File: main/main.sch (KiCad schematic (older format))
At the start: 9 parts

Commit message: picked microcontroller - stm32f401RETx, started schematic, made LED array
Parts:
- removed G1: DOW, william_logos:dow_logo_10mm, symbol william_logos:DOW
- removed G2: MEC, william_logos:mec_small, symbol william_logos:MEC
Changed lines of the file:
@@
 $Descr A4 11693 8268
 encoding utf-8
-Sheet 1 1
+Sheet 1 3
 Title ""
 Date ""
@@
 $EndComp
 $Comp
-L william_logos:DOW G1
-U 1 1 5D9BA876
-P 5800 6700
-F 0 "G1" H 5825 6746 50  0000 L CNN
-F 1 "DOW" H 5825 6655 50  0000 L CNN
-F 2 "william_logos:dow_logo_10mm" H 5800 6800 50  0001 C CNN
-F 3 "" H 5800 6800 50  0001 C CNN
-	1    5800 6700
-	1    0    0    -1
-$EndComp
-$Comp
-L william_logos:MEC G2
-U 1 1 5D9BAA57
-P 5800 6900
-F 0 "G2" H 5825 6946 50  0000 L CNN
-F 1 "MEC" H 5825 6855 50  0000 L CNN
-F 2 "william_logos:mec_small" H 5800 6950 50  0001 C CNN
-F 3 "" H 5800 6950 50  0001 C CNN
-	1    5800 6900
-	1    0    0    -1
-$EndComp
-$Comp
 L william_dfa:Fiducial FID3
 U 1 1 5D9BDAFA
@@
 	1    0    0    -1
 $EndComp
+$Sheet
+S 7500 3250 700  500
+U 5DEECD42
+F0 "LEDs" 50
+F1 "led_array.sch" 50
+F2 "5V" I L 7500 3350 50
+F3 "DIN" I L 7500 3500 50
+F4 "DOUT" O R 8200 3500 50
+F5 "GND" O L 7500 3650 50
+$EndSheet
+$Sheet
+S 3950 2050 1950 1000
+U 5F8F0BCD
+F0 "mic" 50
+F1 "../subs/stm32f401rbXX.sch" 50
+$EndSheet
 $EndSCHEMATC

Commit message: started layout to see if practical
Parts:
- removed FID1, FID2, FID3: Fiducial, Fiducial:Fiducial_1mm_Dia_2mm_Outer, symbol william_dfa:Fiducial
- added BT1: RTC battery, william_batteries:Keystone_3034_1x20mm-CoinCell, symbol Device:Battery_Cell
- added C1, C3: 100N, Capacitor_SMD:C_0603_1608Metric, symbol Device:C
- added C2: 10N, Capacitor_SMD:C_0603_1608Metric, symbol Device:C
- added C4: 10U, Capacitor_SMD:C_0603_1608Metric, symbol Device:C
- added J1: USB_B_Micro, Connector_USB:USB_Micro-B_GCT_USB3076-30-A, symbol Connector:USB_B_Micro
- added SW1, SW2, SW3, SW4, SW5, SW6: SW_SPST, Button_Switch_SMD:SW_Push_1P1T_NO_6x6mm_H9.5mm, symbol Switch:SW_SPST
- added U1: AP1117-33, Package_TO_SOT_SMD:SOT-223-3_TabPin2, symbol Regulator_Linear:AP1117-33
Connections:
- net labels added: +3V3, +5V, +BATT, GND, SWITCH0, SWITCH1, SWITCH2, SWITCH3, SWITCH4, SWITCH5
- wire segments 0 -> 55
- no-connect marks 0 -> 4

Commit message: most components
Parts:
- removed C2: 10N, Capacitor_SMD:C_0603_1608Metric, symbol Device:C
- C1, C3, C4: footprint Capacitor_SMD:C_0603_1608Metric -> Capacitor_SMD:C_0402_1005Metric
- H1, H2, H3, H4: footprint MountingHole:MountingHole_3mm_Pad_Via -> MountingHole:MountingHole_2.1mm
- SW1, SW2, SW3, SW4, SW5, SW6: footprint Button_Switch_SMD:SW_Push_1P1T_NO_6x6mm_H9.5mm -> william_switch:KAN4562-0501C
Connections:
- wire segments 55 -> 53
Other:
- note added: "brightness"
- note added: "hour+"
- note added: "hour-"
- note added: "min+"
- note added: "min-"
- note added: "mode"
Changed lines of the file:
@@
 $Descr A4 11693 8268
 encoding utf-8
-Sheet 1 3
+Sheet 1 4
 Title ""
 Date ""
@@
 F 0 "H1" H 6400 6746 50  0000 L CNN
 F 1 "MountingHole" H 6400 6655 50  0000 L CNN
-F 2 "MountingHole:MountingHole_3mm_Pad_Via" H 6300 6700 50  0001 C CNN
+F 2 "MountingHole:MountingHole_2.1mm" H 6300 6700 50  0001 C CNN
 F 3 "~" H 6300 6700 50  0001 C CNN
 	1    6300 6700
@@
 F 0 "H2" H 6400 7046 50  0000 L CNN
 F 1 "MountingHole" H 6400 6955 50  0000 L CNN
-F 2 "MountingHole:MountingHole_3mm_Pad_Via" H 6300 7000 50  0001 C CNN
+F 2 "MountingHole:MountingHole_2.1mm" H 6300 7000 50  0001 C CNN
 F 3 "~" H 6300 7000 50  0001 C CNN
 	1    6300 7000
@@
 F 0 "H3" H 6400 7346 50  0000 L CNN
 F 1 "MountingHole" H 6400 7255 50  0000 L CNN
-F 2 "MountingHole:MountingHole_3mm_Pad_Via" H 6300 7300 50  0001 C CNN
+F 2 "MountingHole:MountingHole_2.1mm" H 6300 7300 50  0001 C CNN
 F 3 "~" H 6300 7300 50  0001 C CNN
 	1    6300 7300
@@
 F 0 "H4" H 6400 7646 50  0000 L CNN
 F 1 "MountingHole" H 6400 7555 50  0000 L CNN
-F 2 "MountingHole:MountingHole_3mm_Pad_Via" H 6300 7600 50  0001 C CNN
+F 2 "MountingHole:MountingHole_2.1mm" H 6300 7600 50  0001 C CNN
 F 3 "~" H 6300 7600 50  0001 C CNN
 	1    6300 7600
@@
 F5 "GND" O L 6850 3650 50
 $EndSheet
-$Sheet
-S 4400 3150 1250 1150
-U 5F8F0BCD
-F0 "mic" 50
-F1 "../subs/stm32f401rbXX.sch" 50
-F2 "3V3" I L 4400 3250 50
-F3 "GND" I L 4400 4200 50
-F4 "VBAT" I L 4400 3350 50
-F5 "LED_DATA_OUT" O R 5650 3500 50
-F6 "SWITCH0" I L 4400 3500 50
-F7 "SWITCH1" I L 4400 3600 50
-F8 "SWITCH2" I L 4400 3700 50
-F9 "SWITCH3" I L 4400 3800 50
-F10 "SWITCH4" I L 4400 3900 50
-F11 "SWITCH5" I L 4400 4000 50
-$EndSheet
 $Comp
 L Device:Battery_Cell BT1
@@
 $EndComp
 $Comp
-L Device:C C2
-U 1 1 5F9F0D5F
-P 3200 1250
-F 0 "C2" H 3315 1296 50  0000 L CNN
-F 1 "10N" H 3315 1205 50  0000 L CNN
-F 2 "Capacitor_SMD:C_0603_1608Metric" H 3238 1100 50  0001 C CNN
-F 3 "~" H 3200 1250 50  0001 C CNN
-	1    3200 1250
-	1    0    0    -1
-$EndComp
-$Comp
 L Device:C C1
 U 1 1 5F9F1B83
@@
 F 0 "C1" H 2915 1296 50  0000 L CNN
 F 1 "100N" H 2915 1205 50  0000 L CNN
-F 2 "Capacitor_SMD:C_0603_1608Metric" H 2838 1100 50  0001 C CNN
+F 2 "Capacitor_SMD:C_0402_1005Metric" H 2838 1100 50  0001 C CNN
 F 3 "~" H 2800 1250 50  0001 C CNN
 	1    2800 1250
@@
 F 0 "C3" H 4215 1296 50  0000 L CNN
 F 1 "100N" H 4215 1205 50  0000 L CNN
-F 2 "Capacitor_SMD:C_0603_1608Metric" H 4138 1100 50  0001 C CNN
+F 2 "Capacitor_SMD:C_0402_1005Metric" H 4138 1100 50  0001 C CNN
 F 3 "~" H 4100 1250 50  0001 C CNN
 	1    4100 1250
@@
 F 0 "C4" H 4665 1296 50  0000 L CNN
 F 1 "10U" H 4665 1205 50  0000 L CNN
-F 2 "Capacitor_SMD:C_0603_1608Metric" H 4588 1100 50  0001 C CNN
+F 2 "Capacitor_SMD:C_0402_1005Metric" H 4588 1100 50  0001 C CNN
 F 3 "~" H 4550 1250 50  0001 C CNN
 	1    4550 1250
@@
 	1    0    0    -1
 $EndComp
-Wire Wire Line
-	2800 1400 3200 1400
-Connection ~ 3200 1400
-Wire Wire Line
-	3200 1400 3650 1400
 Connection ~ 3650 1400
 Wire Wire Line
@@
 Wire Wire Line
 	2800 1000 2800 1100
-Wire Wire Line
-	3350 1100 3200 1100
 Connection ~ 2800 1100
-Connection ~ 3200 1100
-Wire Wire Line
-	3200 1100 2800 1100
 $Comp
 L power:+3V3 #PWR011
@@
 $EndComp
 $Comp
-L Switch:SW_SPST SW6
-U 1 1 5FA1FE73
-P 1350 5900
-F 0 "SW6" H 1350 6135 50  0000 C CNN
-F 1 "SW_SPST" H 1350 6044 50  0000 C CNN
-F 2 "Button_Switch_SMD:SW_Push_1P1T_NO_6x6mm_H9.5mm" H 1350 5900 50  0001 C CNN
-F 3 "~" H 1350 5900 50  0001 C CNN
-	1    1350 5900
-	1    0    0    -1
-$EndComp
-$Comp
-L Switch:SW_SPST SW5
-U 1 1 5FA1FE69
-P 1350 5500
-F 0 "SW5" H 1350 5735 50  0000 C CNN
-F 1 "SW_SPST" H 1350 5644 50  0000 C CNN
-F 2 "Button_Switch_SMD:SW_Push_1P1T_NO_6x6mm_H9.5mm" H 1350 5500 50  0001 C CNN
-F 3 "~" H 1350 5500 50  0001 C CNN
-	1    1350 5500
-	1    0    0    -1
-$EndComp
-$Comp
-L Switch:SW_SPST SW4
-U 1 1 5FA1E15D
-P 1350 5100
-F 0 "SW4" H 1350 5335 50  0000 C CNN
-F 1 "SW_SPST" H 1350 5244 50  0000 C CNN
-F 2 "Button_Switch_SMD:SW_Push_1P1T_NO_6x6mm_H9.5mm" H 1350 5100 50  0001 C CNN
-F 3 "~" H 1350 5100 50  0001 C CNN
-	1    1350 5100
-	1    0    0    -1
-$EndComp
-$Comp
-L Switch:SW_SPST SW3
-U 1 1 5FA1E153
-P 1350 4700
-F 0 "SW3" H 1350 4935 50  0000 C CNN
-F 1 "SW_SPST" H 1350 4844 50  0000 C CNN
-F 2 "Button_Switch_SMD:SW_Push_1P1T_NO_6x6mm_H9.5mm" H 1350 4700 50  0001 C CNN
-F 3 "~" H 1350 4700 50  0001 C CNN
-	1    1350 4700
-	1    0    0    -1
-$EndComp
-$Comp
-L Switch:SW_SPST SW2
-U 1 1 5FA1CE3B
-P 1350 4300
-F 0 "SW2" H 1350 4535 50  0000 C CNN
-F 1 "SW_SPST" H 1350 4444 50  0000 C CNN
-F 2 "Button_Switch_SMD:SW_Push_1P1T_NO_6x6mm_H9.5mm" H 1350 4300 50  0001 C CNN
-F 3 "~" H 1350 4300 50  0001 C CNN
-	1    1350 4300
-	1    0    0    -1
-$EndComp
-$Comp
 L Switch:SW_SPST SW1
 U 1 1 5FA1CA8C
@@
 F 0 "SW1" H 1350 4135 50  0000 C CNN
 F 1 "SW_SPST" H 1350 4044 50  0000 C CNN
-F 2 "Button_Switch_SMD:SW_Push_1P1T_NO_6x6mm_H9.5mm" H 1350 3900 50  0001 C CNN
+F 2 "william_switch:KAN4562-0501C" H 1350 3900 50  0001 C CNN
 F 3 "~" H 1350 3900 50  0001 C CNN
 	1    1350 3900
@@
 Text Label 3850 3800 0    50   ~ 0
 SWITCH3
-Text Label 3850 3900 0    50   ~ 0
-SWITCH4
-Text Label 3850 4000 0    50   ~ 0
-SWITCH5
 Wire Wire Line
 	4400 3500 3850 3500
@@
 Wire Wire Line
 	3850 3800 4400 3800
-Wire Wire Line
-	4400 3900 3850 3900
-Wire Wire Line
-	3850 4000 4400 4000
 NoConn ~ 1650 1350
 NoConn ~ 1650 1450
@@
 	1    0    0    -1
 $EndComp
+$Sheet
+S 4400 3150 1250 1150
+U 5F8F0BCD
+F0 "mic" 50
+F1 "../subs/STM32F401CBUxX.sch" 50
+F2 "3V3" I L 4400 3250 50
+F3 "GND" I L 4400 4200 50
+F4 "VBAT" I L 4400 3350 50
+F5 "LED_DATA_OUT" O R 5650 3500 50
+F6 "SWITCH0" I L 4400 3500 50
+F7 "SWITCH1" I L 4400 3600 50
+F8 "SWITCH2" I L 4400 3700 50
+F9 "SWITCH3" I L 4400 3800 50
+F10 "SWITCH4" I L 4400 3900 50
+F11 "SWITCH5" I L 4400 4000 50
+$EndSheet
+Text Notes 2300 3900 0    50   ~ 0
+hour+
+Text Notes 2250 4700 0    50   ~ 0
+min+
+Text Notes 2250 5450 0    50   ~ 0
+mode
+Text Notes 2250 5900 0    50   ~ 0
+brightness
+Wire Wire Line
+	3850 4000 4400 4000
+Wire Wire Line
+	4400 3900 3850 3900
+Text Label 3850 4000 0    50   ~ 0
+SWITCH5
+Text Label 3850 3900 0    50   ~ 0
+SWITCH4
+Text Notes 2250 4300 0    50   ~ 0
+hour-
+Text Notes 2250 5050 0    50   ~ 0
+min-
+$Comp
+L Switch:SW_SPST SW2
+U 1 1 60E0254F
+P 1350 4300
+F 0 "SW2" H 1350 4535 50  0000 C CNN
+F 1 "SW_SPST" H 1350 4444 50  0000 C CNN
+F 2 "william_switch:KAN4562-0501C" H 1350 4300 50  0001 C CNN
+F 3 "~" H 1350 4300 50  0001 C CNN
+	1    1350 4300
+	1    0    0    -1
+$EndComp
+$Comp
+L Switch:SW_SPST SW3
+U 1 1 60E0418F
+P 1350 4700
+F 0 "SW3" H 1350 4935 50  0000 C CNN
+F 1 "SW_SPST" H 1350 4844 50  0000 C CNN
+F 2 "william_switch:KAN4562-0501C" H 1350 4700 50  0001 C CNN
+F 3 "~" H 1350 4700 50  0001 C CNN
+	1    1350 4700
+	1    0    0    -1
+$EndComp
+$Comp
+L Switch:SW_SPST SW4
+U 1 1 60E04199
+P 1350 5100
+F 0 "SW4" H 1350 5335 50  0000 C CNN
+F 1 "SW_SPST" H 1350 5244 50  0000 C CNN
+F 2 "william_switch:KAN4562-0501C" H 1350 5100 50  0001 C CNN
+F 3 "~" H 1350 5100 50  0001 C CNN
+	1    1350 5100
+	1    0    0    -1
+$EndComp
+$Comp
+L Switch:SW_SPST SW5
+U 1 1 60E05E72
+P 1350 5500
+F 0 "SW5" H 1350 5735 50  0000 C CNN
+F 1 "SW_SPST" H 1350 5644 50  0000 C CNN
+F 2 "william_switch:KAN4562-0501C" H 1350 5500 50  0001 C CNN
+F 3 "~" H 1350 5500 50  0001 C CNN
+	1    1350 5500
+	1    0    0    -1
+$EndComp
+$Comp
+L Switch:SW_SPST SW6
+U 1 1 60E05E7C
+P 1350 5900
+F 0 "SW6" H 1350 6135 50  0000 C CNN
+F 1 "SW_SPST" H 1350 6044 50  0000 C CNN
+F 2 "william_switch:KAN4562-0501C" H 1350 5900 50  0001 C CNN
+F 3 "~" H 1350 5900 50  0001 C CNN
+	1    1350 5900
+	1    0    0    -1
+$EndComp
+Wire Wire Line
+	2800 1100 3350 1100
+Wire Wire Line
+	2800 1400 3650 1400
 $EndSCHEMATC

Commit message: started layout.  Trying to figure out star power topology into MCU
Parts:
- removed BT1: RTC battery, william_batteries:Keystone_3034_1x20mm-CoinCell, symbol Device:Battery_Cell
- removed U1: AP1117-33, Package_TO_SOT_SMD:SOT-223-3_TabPin2, symbol Regulator_Linear:AP1117-33
- added BT1: CR2032-BS-6-1, william_batteries:CR2032-BS-6-1, symbol william_connectors:CR2032-BS-6-1
- added U1: LN6206P332MR-G, Package_TO_SOT_SMD:SOT-23, symbol william_dc_ldo:LN6206P332MR-G
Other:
- note added: "LCSC pn:\nC141407"
- note added: "RTC cell"
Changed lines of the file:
@@
 $EndSheet
-$Comp
-L Device:Battery_Cell BT1
-U 1 1 5F9E5BE0
-P 1200 2750
-F 0 "BT1" H 1318 2846 50  0000 L CNN
-F 1 "RTC battery" H 1318 2755 50  0000 L CNN
-F 2 "william_batteries:Keystone_3034_1x20mm-CoinCell" V 1200 2810 50  0001 C CNN
-F 3 "~" V 1200 2810 50  0001 C CNN
-	1    1200 2750
-	1    0    0    -1
-$EndComp
 $Comp
 L Connector:USB_B_Micro J1
@@
 F 3 "" H 1200 2850 50  0001 C CNN
 	1    1200 2850
-	1    0    0    -1
-$EndComp
-$Comp
-L Regulator_Linear:AP1117-33 U1
-U 1 1 5F9EFF5E
-P 3650 1100
-F 0 "U1" H 3650 1342 50  0000 C CNN
-F 1 "AP1117-33" H 3650 1251 50  0000 C CNN
-F 2 "Package_TO_SOT_SMD:SOT-223-3_TabPin2" H 3650 1300 50  0001 C CNN
-F 3 "http://www.diodes.com/datasheets/AP1117.pdf" H 3750 850 50  0001 C CNN
-	1    3650 1100
 	1    0    0    -1
 $EndComp
@@
 Wire Wire Line
 	2800 1400 3650 1400
+Text Notes 4150 1600 0    50   ~ 0
+LCSC pn:\nC141407
+$Comp
+L william_dc_ldo:LN6206P332MR-G U1
+U 1 1 5DF1CFB8
+P 3650 1150
+F 0 "U1" H 3650 1442 50  0000 C CNN
+F 1 "LN6206P332MR-G" H 3650 1351 50  0000 C CNN
+F 2 "Package_TO_SOT_SMD:SOT-23" H 3800 1500 50  0001 C CNN
+F 3 "https://datasheet.lcsc.com/szlcsc/1810311908_NATLINEAR-LN6206P332MR-G_C141407.pdf" H 3800 1500 50  0001 C CNN
+	1    3650 1150
+	1    0    0    -1
+$EndComp
+Text Notes 1550 2450 0    50   ~ 0
+RTC cell
+$Comp
+L william_connectors:CR2032-BS-6-1 BT1
+U 1 1 5DF2AF87
+P 1200 2750
+F 0 "BT1" H 1318 2846 50  0000 L CNN
+F 1 "CR2032-BS-6-1" H 1318 2755 50  0000 L CNN
+F 2 "william_batteries:CR2032-BS-6-1" V 1200 2810 50  0001 C CNN
+F 3 "https://datasheet.lcsc.com/szlcsc/1811061923_Q-J-CR2032-BS-6-1_C70377.pdf" V 1200 2810 50  0001 C CNN
+	1    1200 2750
+	1    0    0    -1
+$EndComp
 $EndSCHEMATC

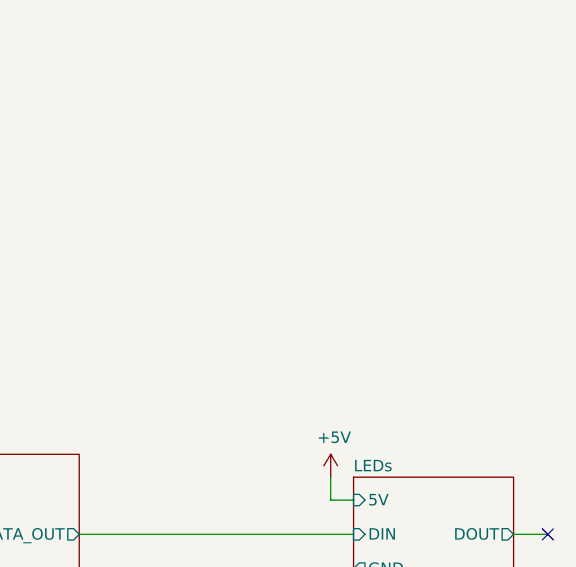
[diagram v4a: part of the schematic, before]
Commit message: most layout finished?  not super happy w/ star topology, but not lots of noise from this system, so probably just fine. now to add caps...
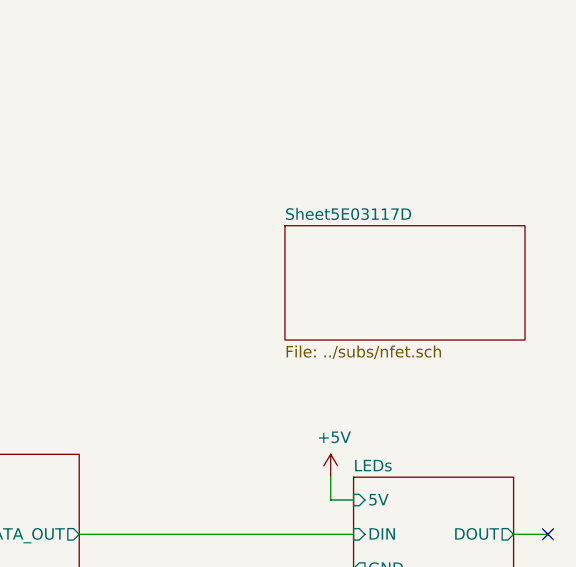
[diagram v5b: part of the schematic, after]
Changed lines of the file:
@@
 $Descr A4 11693 8268
 encoding utf-8
-Sheet 1 4
+Sheet 1 5
 Title ""
 Date ""
@@
 	1    0    0    -1
 $EndComp
+$Sheet
+S 6550 2150 1050 500
+U 5E03117E
+F0 "Sheet5E03117D" 50
+F1 "../subs/nfet.sch" 50
+$EndSheet
 $EndSCHEMATC
